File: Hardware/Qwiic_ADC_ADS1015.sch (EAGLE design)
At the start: 25 parts, among them J4 Screw Pin Terminals, U1 ADS1015

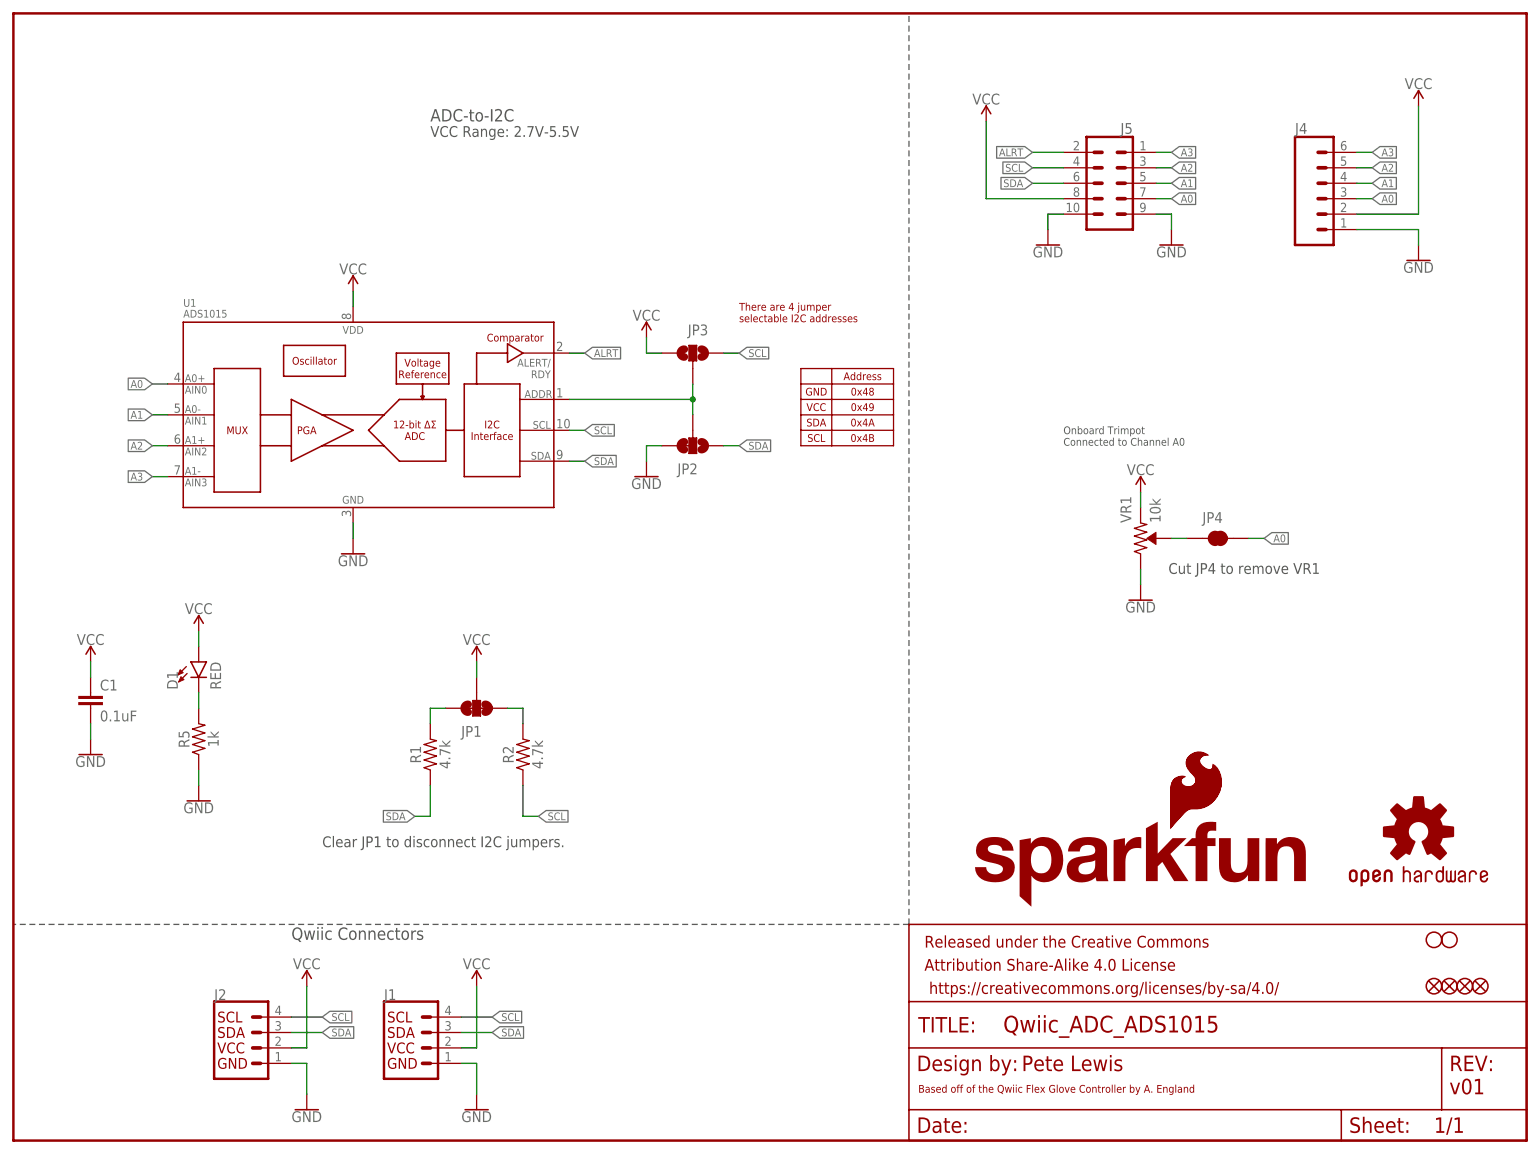
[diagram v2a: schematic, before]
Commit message: Group design review changes
Moved Trimpot to A3 - so that initial use case can use A0 "as usual".
Improved address jumper labeling
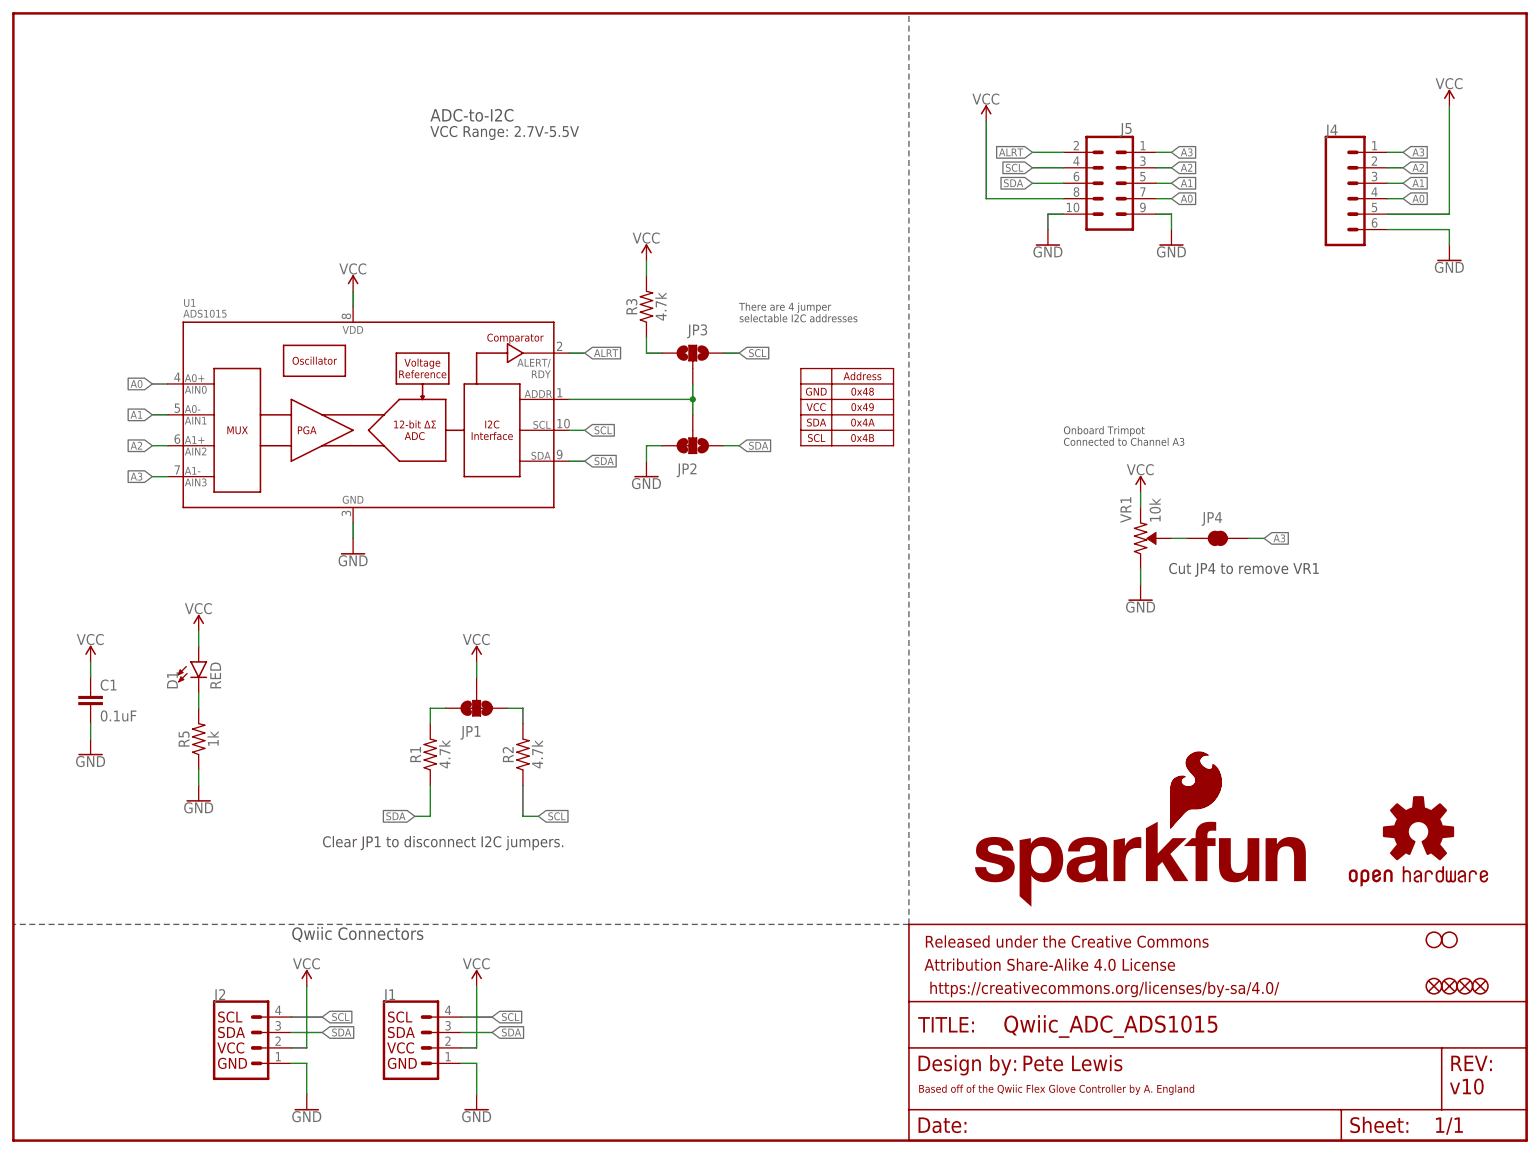
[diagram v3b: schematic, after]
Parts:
- added R3: 4.7k, SparkFun-Resistors:4.7KOHM-0603-1/10W-1%
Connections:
- new net N$3: JP3.1, R3.1
- net A0: now also J4.4; no longer J4.3, JP4.2
- net A1: now also J4.3; no longer J4.4
- net A2: now also J4.2; no longer J4.5
- net A3: now also J4.1, JP4.2; no longer J4.6
- net GND: now also J4.6; no longer J4.1
- net VCC: now also J4.5, R3.2; no longer J4.2, JP3.1
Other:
- note added: "Onboard Trimpot Connected to Channel A3"
- note added: "v10"
- note removed: "Onboard Trimpot Connected to Channel A0"
- note removed: "v01"
- moved on the sheet: J4

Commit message: Checklist changes pre double-check
Cleaned up schematic.
Added note for alert ready active high or low.
Adjusted some small stuff for better ground pour flow.
Added SS path on layer 47.
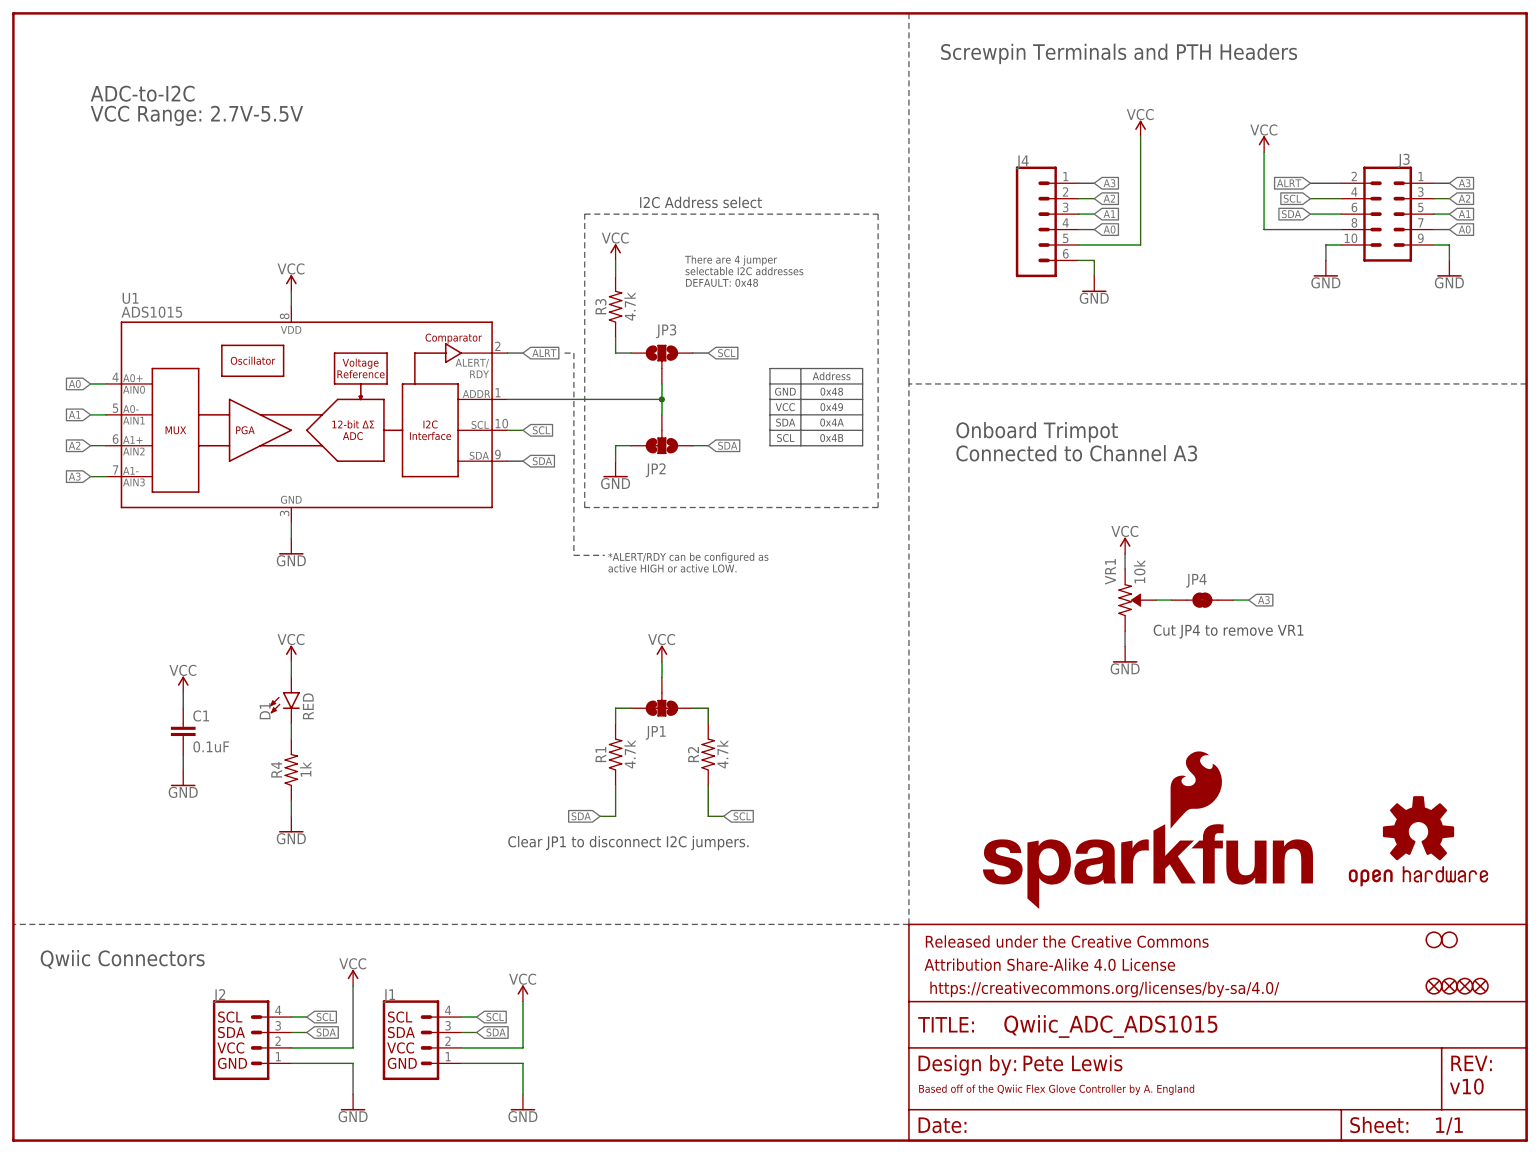
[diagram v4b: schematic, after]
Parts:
- removed J5: (no value), SparkFun-Connectors:CONN_05X2NO_SILK
- removed R5: 1k, SparkFun-Resistors:1KOHM-0603-1/10W-1%
- added J3: (no value), SparkFun-Connectors:CONN_05X2NO_SILK
- added R4: 1k, SparkFun-Resistors:1KOHM-0603-1/10W-1%
- J4: value Screw Pin Terminals -> Screw Pin
- LOGO1: value SFE_LOGO_NAME_FLAME.1_INCH -> SFE_LOGO_NAME.1_INCH; device SparkFun-Aesthetics:SFE_LOGO_NAME_FLAME.1_INCH -> SparkFun-Aesthetics:SFE_LOGO_NAME.1_INCH
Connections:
- net A0: now also J3.7; no longer J5.7
- net A1: now also J3.5; no longer J5.5
- net A2: now also J3.3; no longer J5.3
- net A3: now also J3.1; no longer J5.1
- net ALRT: now also J3.2; no longer J5.2
- net GND: now also J3.10, J3.9, R4.1; no longer J5.10, J5.9, R5.1
- net N$2: now also R4.2; no longer R5.2
- net SCL: now also J3.4; no longer J5.4
- net SDA: now also J3.6; no longer J5.6
- net VCC: now also J3.8; no longer J5.8
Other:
- note added: "*ALERT/RDY can be configured as active HIGH or active LOW."
- note added: "I2C Address select"
- note added: "Screwpin Terminals and PTH Headers"
- note added: "There are 4 jumper selectable I2C addresses DEFAULT: 0x48"
- note removed: "There are 4 jumper selectable I2C addresses"
- moved on the sheet: C1, D1, J4, JP1, JP2, JP3, JP4, R1, R2, R3, U1, VR1
